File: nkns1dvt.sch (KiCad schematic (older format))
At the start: 70 parts, among them J1 MJ-4PP-9, J2 SERIAL_LED, SW1 SW_RESET, SW10 SW_PUSH, SW11 SW_PUSH, SW12 SW_PUSH, SW13 SW_PUSH, SW14 SW_PUSH, SW15 SW_PUSH, SW16 SW_PUSH, SW17 SW_PUSH, SW18 SW_PUSH, SW19 SW_PUSH, SW2 SW_PUSH, SW20 SW_PUSH, SW21 SW_PUSH, SW22 SW_PUSH, SW23 SW_PUSH, SW24 SW_PUSH, SW25 SW_PUSH, SW26 SW_PUSH, SW27 SW_PUSH, SW28 SW_PUSH, SW29 SW_PUSH, SW3 SW_PUSH, SW30 SW_PUSH, SW31 SW_PUSH, SW32 SW_PUSH, SW33 SW_PUSH, SW34 SW_PUSH, SW4 SW_PUSH, SW5 SW_PUSH, SW6 SW_PUSH, SW7 SW_PUSH, SW8 SW_PUSH, SW9 SW_PUSH, U1 ProMicro

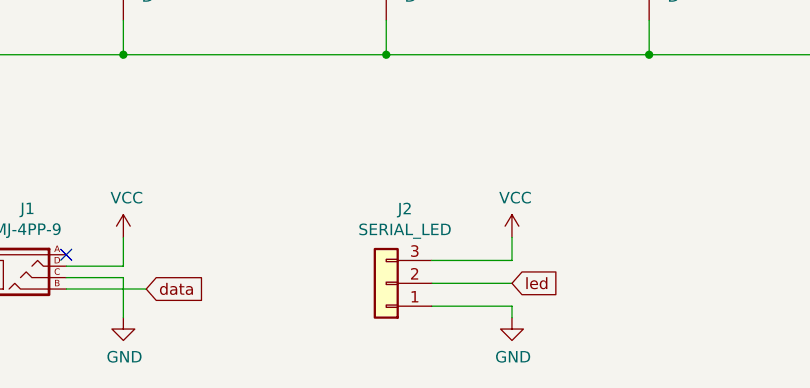
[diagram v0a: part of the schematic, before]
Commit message: Modify LED. Add GND/VCC route.
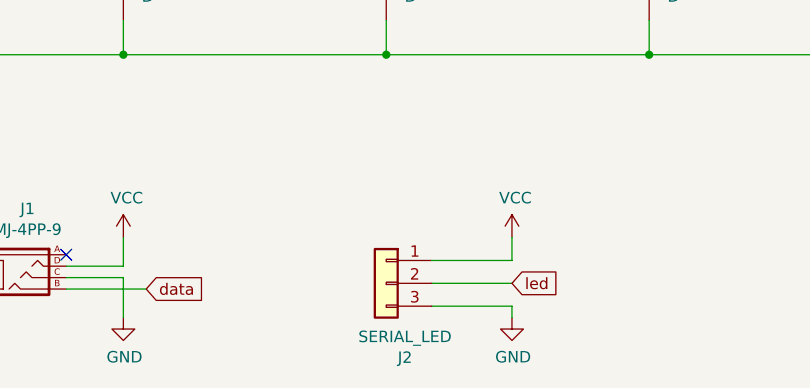
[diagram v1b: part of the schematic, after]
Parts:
- U1: footprint kbd:ProMicro_v3.5 -> Keebio-Parts:ArduinoProMicro-ZigZag
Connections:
- net GND: now also J2.3 (Pin_3); no longer J2.1 (Pin_1)
- net VCC: now also J2.1 (Pin_1); no longer J2.3 (Pin_3)
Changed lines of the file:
@@
 encoding utf-8
 Sheet 1 1
-Title "nkns66 DVT"
+Title "nkns0 dvt (L)"
 Date "2020-11-03"
 Rev "0.1"
@@
 F 0 "U1" H 9500 3087 60  0000 C CNN
 F 1 "ProMicro" H 9500 2981 60  0000 C CNN
-F 2 "kbd:ProMicro_v3.5" H 9600 1200 60  0001 C CNN
+F 2 "Keebio-Parts:ArduinoProMicro-ZigZag" H 9600 1200 60  0001 C CNN
 F 3 "" H 9600 1200 60  0000 C CNN
 	1    9500 2250
@@
 led
 NoConn ~ 10200 2800
+Wire Wire Line
+	4150 6950 4500 6950
+Wire Wire Line
+	4150 7050 4500 7050
+Wire Wire Line
+	4500 7050 4500 7100
+Wire Wire Line
+	4150 6850 4500 6850
+Wire Wire Line
+	4500 6850 4500 6750
 $Comp
 L Connector_Generic:Conn_01x03 J2
@@
 F 3 "~" H 3950 6950 50  0001 C CNN
 	1    3950 6950
-	-1   0    0    1
-$EndComp
-Wire Wire Line
-	4150 6950 4500 6950
-Wire Wire Line
-	4150 7050 4500 7050
-Wire Wire Line
-	4500 7050 4500 7100
-Wire Wire Line
-	4150 6850 4500 6850
-Wire Wire Line
-	4500 6850 4500 6750
+	-1   0    0    -1
+$EndComp
 $EndSCHEMATC

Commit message: Change to reversible.
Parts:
- J1: footprint kbd:MJ-4PP-9_1side -> kbd:MJ-4PP-9
- J2: footprint kbd:StripLED_1side -> kbd:StripLED_rev
- SW1: footprint kbd:ResetSW_1side -> kbd:ResetSW
- SW10, SW11, SW12, SW13, SW14, SW15, SW16, SW17, SW18, SW19, SW2, SW20, SW21, SW22, SW23, SW24, SW25, SW26, SW27, SW28, SW29, SW3, SW30, SW31, SW32, SW33, SW34, SW4, SW5, SW6, SW7, SW8, SW9: footprint kbd:CherryMX_Hotswap -> kbd:CherryMX_MidHeight_Hotswap
- U1: footprint Keebio-Parts:ArduinoProMicro-ZigZag -> kbd:ProMicro_v2
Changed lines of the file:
@@
 F 0 "SW4" H 3650 1655 50  0000 C CNN
 F 1 "SW_PUSH" H 3650 1564 50  0000 C CNN
-F 2 "kbd:CherryMX_Hotswap" H 3650 1400 50  0001 C CNN
+F 2 "kbd:CherryMX_MidHeight_Hotswap" H 3650 1400 50  0001 C CNN
 F 3 "" H 3650 1400 50  0000 C CNN
 	1    3650 1400
@@
 F 0 "SW3" H 2500 1655 50  0000 C CNN
 F 1 "SW_PUSH" H 2500 1564 50  0000 C CNN
-F 2 "kbd:CherryMX_Hotswap" H 2500 1400 50  0001 C CNN
+F 2 "kbd:CherryMX_MidHeight_Hotswap" H 2500 1400 50  0001 C CNN
 F 3 "" H 2500 1400 50  0000 C CNN
 	1    2500 1400
@@
 F 0 "SW2" H 1350 1655 50  0000 C CNN
 F 1 "SW_PUSH" H 1350 1564 50  0000 C CNN
-F 2 "kbd:CherryMX_Hotswap" H 1350 1400 50  0001 C CNN
+F 2 "kbd:CherryMX_MidHeight_Hotswap" H 1350 1400 50  0001 C CNN
 F 3 "" H 1350 1400 50  0000 C CNN
 	1    1350 1400
@@
 F 0 "SW10" H 3650 2655 50  0000 C CNN
 F 1 "SW_PUSH" H 3650 2564 50  0000 C CNN
-F 2 "kbd:CherryMX_Hotswap" H 3650 2400 50  0001 C CNN
+F 2 "kbd:CherryMX_MidHeight_Hotswap" H 3650 2400 50  0001 C CNN
 F 3 "" H 3650 2400 50  0000 C CNN
 	1    3650 2400
@@
 F 0 "SW9" H 2500 2655 50  0000 C CNN
 F 1 "SW_PUSH" H 2500 2564 50  0000 C CNN
-F 2 "kbd:CherryMX_Hotswap" H 2500 2400 50  0001 C CNN
+F 2 "kbd:CherryMX_MidHeight_Hotswap" H 2500 2400 50  0001 C CNN
 F 3 "" H 2500 2400 50  0000 C CNN
 	1    2500 2400
@@
 F 0 "SW8" H 1350 2655 50  0000 C CNN
 F 1 "SW_PUSH" H 1350 2564 50  0000 C CNN
-F 2 "kbd:CherryMX_Hotswap" H 1350 2400 50  0001 C CNN
+F 2 "kbd:CherryMX_MidHeight_Hotswap" H 1350 2400 50  0001 C CNN
 F 3 "" H 1350 2400 50  0000 C CNN
 	1    1350 2400
@@
 F 0 "SW16" H 3650 3655 50  0000 C CNN
 F 1 "SW_PUSH" H 3650 3564 50  0000 C CNN
-F 2 "kbd:CherryMX_Hotswap" H 3650 3400 50  0001 C CNN
+F 2 "kbd:CherryMX_MidHeight_Hotswap" H 3650 3400 50  0001 C CNN
 F 3 "" H 3650 3400 50  0000 C CNN
 	1    3650 3400
@@
 F 0 "SW15" H 2500 3655 50  0000 C CNN
 F 1 "SW_PUSH" H 2500 3564 50  0000 C CNN
-F 2 "kbd:CherryMX_Hotswap" H 2500 3400 50  0001 C CNN
+F 2 "kbd:CherryMX_MidHeight_Hotswap" H 2500 3400 50  0001 C CNN
 F 3 "" H 2500 3400 50  0000 C CNN
 	1    2500 3400
@@
 F 0 "SW14" H 1350 3655 50  0000 C CNN
 F 1 "SW_PUSH" H 1350 3564 50  0000 C CNN
-F 2 "kbd:CherryMX_Hotswap" H 1350 3400 50  0001 C CNN
+F 2 "kbd:CherryMX_MidHeight_Hotswap" H 1350 3400 50  0001 C CNN
 F 3 "" H 1350 3400 50  0000 C CNN
 	1    1350 3400
@@
 F 0 "SW22" H 3650 4705 50  0000 C CNN
 F 1 "SW_PUSH" H 3650 4614 50  0000 C CNN
-F 2 "kbd:CherryMX_Hotswap" H 3650 4450 50  0001 C CNN
+F 2 "kbd:CherryMX_MidHeight_Hotswap" H 3650 4450 50  0001 C CNN
 F 3 "" H 3650 4450 50  0000 C CNN
 	1    3650 4450
@@
 F 0 "SW21" H 2500 4705 50  0000 C CNN
 F 1 "SW_PUSH" H 2500 4614 50  0000 C CNN
-F 2 "kbd:CherryMX_Hotswap" H 2500 4450 50  0001 C CNN
+F 2 "kbd:CherryMX_MidHeight_Hotswap" H 2500 4450 50  0001 C CNN
 F 3 "" H 2500 4450 50  0000 C CNN
 	1    2500 4450
@@
 F 0 "SW20" H 1350 4705 50  0000 C CNN
 F 1 "SW_PUSH" H 1350 4614 50  0000 C CNN
-F 2 "kbd:CherryMX_Hotswap" H 1350 4450 50  0001 C CNN
+F 2 "kbd:CherryMX_MidHeight_Hotswap" H 1350 4450 50  0001 C CNN
 F 3 "" H 1350 4450 50  0000 C CNN
 	1    1350 4450
@@
 F 0 "SW29" H 3650 5755 50  0000 C CNN
 F 1 "SW_PUSH" H 3650 5664 50  0000 C CNN
-F 2 "kbd:CherryMX_Hotswap" H 3650 5500 50  0001 C CNN
+F 2 "kbd:CherryMX_MidHeight_Hotswap" H 3650 5500 50  0001 C CNN
 F 3 "" H 3650 5500 50  0000 C CNN
 	1    3650 5500
@@
 F 0 "SW28" H 2500 5755 50  0000 C CNN
 F 1 "SW_PUSH" H 2500 5664 50  0000 C CNN
-F 2 "kbd:CherryMX_Hotswap" H 2500 5500 50  0001 C CNN
+F 2 "kbd:CherryMX_MidHeight_Hotswap" H 2500 5500 50  0001 C CNN
 F 3 "" H 2500 5500 50  0000 C CNN
 	1    2500 5500
@@
 F 0 "SW27" H 1350 5755 50  0000 C CNN
 F 1 "SW_PUSH" H 1350 5664 50  0000 C CNN
-F 2 "kbd:CherryMX_Hotswap" H 1350 5500 50  0001 C CNN
+F 2 "kbd:CherryMX_MidHeight_Hotswap" H 1350 5500 50  0001 C CNN
 F 3 "" H 1350 5500 50  0000 C CNN
 	1    1350 5500
@@
 F 0 "SW1" H 10350 4005 50  0000 C CNN
 F 1 "SW_RESET" H 10350 3914 50  0000 C CNN
-F 2 "kbd:ResetSW_1side" H 10350 3750 50  0001 C CNN
+F 2 "kbd:ResetSW" H 10350 3750 50  0001 C CNN
 F 3 "" H 10350 3750 50  0000 C CNN
 	1    10350 3750
@@
 F 0 "SW34" H 9400 5755 50  0000 C CNN
 F 1 "SW_PUSH" H 9400 5664 50  0000 C CNN
-F 2 "kbd:CherryMX_Hotswap" H 9400 5500 50  0001 C CNN
+F 2 "kbd:CherryMX_MidHeight_Hotswap" H 9400 5500 50  0001 C CNN
 F 3 "" H 9400 5500 50  0000 C CNN
 	1    9400 5500
@@
 F 0 "SW33" H 8250 5755 50  0000 C CNN
 F 1 "SW_PUSH" H 8250 5664 50  0000 C CNN
-F 2 "kbd:CherryMX_Hotswap" H 8250 5500 50  0001 C CNN
+F 2 "kbd:CherryMX_MidHeight_Hotswap" H 8250 5500 50  0001 C CNN
 F 3 "" H 8250 5500 50  0000 C CNN
 	1    8250 5500
@@
 F 0 "SW26" H 8250 4705 50  0000 C CNN
 F 1 "SW_PUSH" H 8250 4614 50  0000 C CNN
-F 2 "kbd:CherryMX_Hotswap" H 8250 4450 50  0001 C CNN
+F 2 "kbd:CherryMX_MidHeight_Hotswap" H 8250 4450 50  0001 C CNN
 F 3 "" H 8250 4450 50  0000 C CNN
 	1    8250 4450
@@
 F 0 "SW30" H 4800 5755 50  0000 C CNN
 F 1 "SW_PUSH" H 4800 5664 50  0000 C CNN
-F 2 "kbd:CherryMX_Hotswap" H 4800 5500 50  0001 C CNN
+F 2 "kbd:CherryMX_MidHeight_Hotswap" H 4800 5500 50  0001 C CNN
 F 3 "" H 4800 5500 50  0000 C CNN
 	1    4800 5500
@@
 F 0 "SW31" H 5950 5755 50  0000 C CNN
 F 1 "SW_PUSH" H 5950 5664 50  0000 C CNN
-F 2 "kbd:CherryMX_Hotswap" H 5950 5500 50  0001 C CNN
+F 2 "kbd:CherryMX_MidHeight_Hotswap" H 5950 5500 50  0001 C CNN
 F 3 "" H 5950 5500 50  0000 C CNN
 	1    5950 5500
@@
 F 0 "SW32" H 7100 5755 50  0000 C CNN
 F 1 "SW_PUSH" H 7100 5664 50  0000 C CNN
-F 2 "kbd:CherryMX_Hotswap" H 7100 5500 50  0001 C CNN
+F 2 "kbd:CherryMX_MidHeight_Hotswap" H 7100 5500 50  0001 C CNN
 F 3 "" H 7100 5500 50  0000 C CNN
 	1    7100 5500
@@
 F 0 "SW23" H 4800 4705 50  0000 C CNN
 F 1 "SW_PUSH" H 4800 4614 50  0000 C CNN
-F 2 "kbd:CherryMX_Hotswap" H 4800 4450 50  0001 C CNN
+F 2 "kbd:CherryMX_MidHeight_Hotswap" H 4800 4450 50  0001 C CNN
 F 3 "" H 4800 4450 50  0000 C CNN
 	1    4800 4450
@@
 F 0 "SW24" H 5950 4705 50  0000 C CNN
 F 1 "SW_PUSH" H 5950 4614 50  0000 C CNN
-F 2 "kbd:CherryMX_Hotswap" H 5950 4450 50  0001 C CNN
+F 2 "kbd:CherryMX_MidHeight_Hotswap" H 5950 4450 50  0001 C CNN
 F 3 "" H 5950 4450 50  0000 C CNN
 	1    5950 4450
@@
 F 0 "SW25" H 7100 4705 50  0000 C CNN
 F 1 "SW_PUSH" H 7100 4614 50  0000 C CNN
-F 2 "kbd:CherryMX_Hotswap" H 7100 4450 50  0001 C CNN
+F 2 "kbd:CherryMX_MidHeight_Hotswap" H 7100 4450 50  0001 C CNN
 F 3 "" H 7100 4450 50  0000 C CNN
 	1    7100 4450
@@
 F 0 "SW17" H 4800 3655 50  0000 C CNN
 F 1 "SW_PUSH" H 4800 3564 50  0000 C CNN
-F 2 "kbd:CherryMX_Hotswap" H 4800 3400 50  0001 C CNN
+F 2 "kbd:CherryMX_MidHeight_Hotswap" H 4800 3400 50  0001 C CNN
 F 3 "" H 4800 3400 50  0000 C CNN
 	1    4800 3400
@@
 F 0 "SW18" H 5950 3655 50  0000 C CNN
 F 1 "SW_PUSH" H 5950 3564 50  0000 C CNN
-F 2 "kbd:CherryMX_Hotswap" H 5950 3400 50  0001 C CNN
+F 2 "kbd:CherryMX_MidHeight_Hotswap" H 5950 3400 50  0001 C CNN
 F 3 "" H 5950 3400 50  0000 C CNN
 	1    5950 3400
@@
 F 0 "SW19" H 7100 3655 50  0000 C CNN
 F 1 "SW_PUSH" H 7100 3564 50  0000 C CNN
-F 2 "kbd:CherryMX_Hotswap" H 7100 3400 50  0001 C CNN
+F 2 "kbd:CherryMX_MidHeight_Hotswap" H 7100 3400 50  0001 C CNN
 F 3 "" H 7100 3400 50  0000 C CNN
 	1    7100 3400
@@
 F 0 "SW11" H 4800 2655 50  0000 C CNN
 F 1 "SW_PUSH" H 4800 2564 50  0000 C CNN
-F 2 "kbd:CherryMX_Hotswap" H 4800 2400 50  0001 C CNN
+F 2 "kbd:CherryMX_MidHeight_Hotswap" H 4800 2400 50  0001 C CNN
 F 3 "" H 4800 2400 50  0000 C CNN
 	1    4800 2400
@@
 F 0 "SW12" H 5950 2655 50  0000 C CNN
 F 1 "SW_PUSH" H 5950 2564 50  0000 C CNN
-F 2 "kbd:CherryMX_Hotswap" H 5950 2400 50  0001 C CNN
+F 2 "kbd:CherryMX_MidHeight_Hotswap" H 5950 2400 50  0001 C CNN
 F 3 "" H 5950 2400 50  0000 C CNN
 	1    5950 2400
@@
 F 0 "SW13" H 7100 2655 50  0000 C CNN
 F 1 "SW_PUSH" H 7100 2564 50  0000 C CNN
-F 2 "kbd:CherryMX_Hotswap" H 7100 2400 50  0001 C CNN
+F 2 "kbd:CherryMX_MidHeight_Hotswap" H 7100 2400 50  0001 C CNN
 F 3 "" H 7100 2400 50  0000 C CNN
 	1    7100 2400
@@
 F 0 "SW5" H 4800 1655 50  0000 C CNN
 F 1 "SW_PUSH" H 4800 1564 50  0000 C CNN
-F 2 "kbd:CherryMX_Hotswap" H 4800 1400 50  0001 C CNN
+F 2 "kbd:CherryMX_MidHeight_Hotswap" H 4800 1400 50  0001 C CNN
 F 3 "" H 4800 1400 50  0000 C CNN
 	1    4800 1400
@@
 F 0 "SW6" H 5950 1655 50  0000 C CNN
 F 1 "SW_PUSH" H 5950 1564 50  0000 C CNN
-F 2 "kbd:CherryMX_Hotswap" H 5950 1400 50  0001 C CNN
+F 2 "kbd:CherryMX_MidHeight_Hotswap" H 5950 1400 50  0001 C CNN
 F 3 "" H 5950 1400 50  0000 C CNN
 	1    5950 1400
@@
 F 0 "SW7" H 7100 1655 50  0000 C CNN
 F 1 "SW_PUSH" H 7100 1564 50  0000 C CNN
-F 2 "kbd:CherryMX_Hotswap" H 7100 1400 50  0001 C CNN
+F 2 "kbd:CherryMX_MidHeight_Hotswap" H 7100 1400 50  0001 C CNN
 F 3 "" H 7100 1400 50  0000 C CNN
 	1    7100 1400
@@
 F 0 "U1" H 9500 3087 60  0000 C CNN
 F 1 "ProMicro" H 9500 2981 60  0000 C CNN
-F 2 "Keebio-Parts:ArduinoProMicro-ZigZag" H 9600 1200 60  0001 C CNN
+F 2 "kbd:ProMicro_v2" H 9600 1200 60  0001 C CNN
 F 3 "" H 9600 1200 60  0000 C CNN
 	1    9500 2250
@@
 F 0 "J1" H 2381 7176 50  0000 C CNN
 F 1 "MJ-4PP-9" H 2381 7085 50  0000 C CNN
-F 2 "kbd:MJ-4PP-9_1side" H 2625 7075 50  0001 C CNN
+F 2 "kbd:MJ-4PP-9" H 2625 7075 50  0001 C CNN
 F 3 "~" H 2625 7075 50  0001 C CNN
 	1    2350 6900
@@
 F 0 "J2" H 3868 6625 50  0000 C CNN
 F 1 "SERIAL_LED" H 3868 6716 50  0000 C CNN
-F 2 "kbd:StripLED_1side" H 3950 6950 50  0001 C CNN
+F 2 "kbd:StripLED_rev" H 3950 6950 50  0001 C CNN
 F 3 "~" H 3950 6950 50  0001 C CNN
 	1    3950 6950
